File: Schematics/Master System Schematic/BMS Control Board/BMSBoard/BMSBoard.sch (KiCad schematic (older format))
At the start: 22 parts, among them J1 GLV_PWR, J10 GND_QC, J2 GLV_Signal, J3 Charge_PWR, J4 Charge_Signal, J5 PumpIO, J6 Therm_PWR, J7 Therm_Signal, J8 BMS_PWR, J9 BMS_Signal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

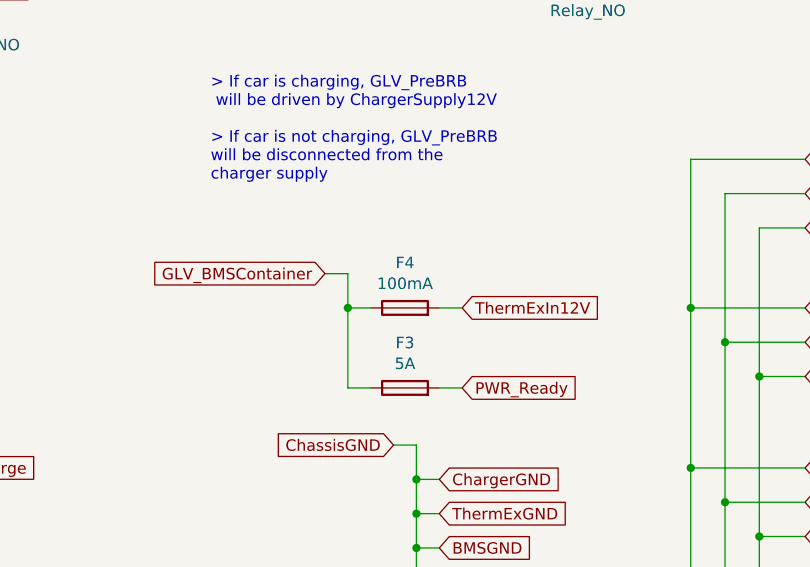
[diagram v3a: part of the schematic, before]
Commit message: Small fuse change
> Removed fuse for thermistor expansion
Version 2.2
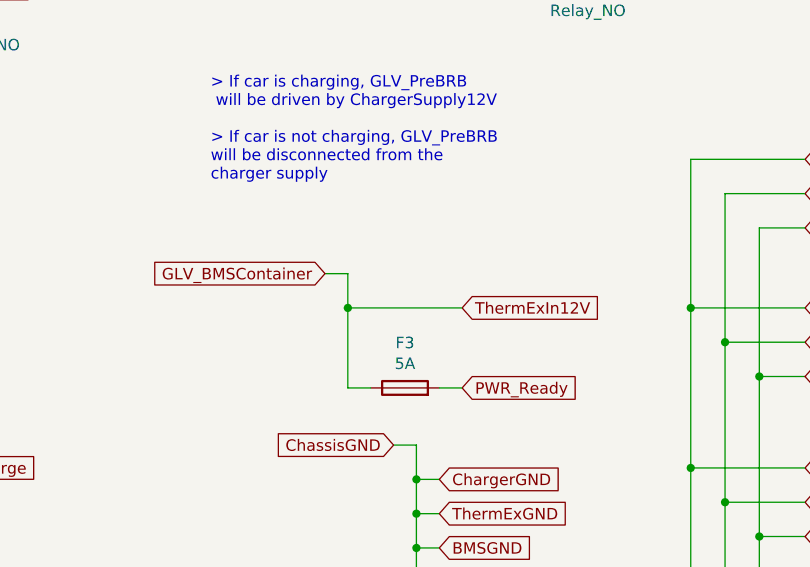
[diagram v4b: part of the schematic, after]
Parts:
- removed F4: 100mA, symbol Device:Fuse
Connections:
- net ThermExIn12V is gone; now on net GLV_BMSContainer: J6.1 (Pin_1)
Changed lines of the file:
@@
 Sheet 1 1
 Title "BMS Control Board"
-Date "2020-11-14"
-Rev "2.1"
+Date "2020-11-19"
+Rev "2.2"
 Comp "Northeastern Electric Racing"
 Comment1 "https://github.com/Northeastern-Electric-Racing/NER"
@@
 	6250 4050 6350 4050
 Wire Wire Line
-	6450 4200 6350 4200
-Wire Wire Line
 	6350 4200 6350 4050
 Text GLabel 6550 4800 0    50   Input ~ 0
@@
 Wire Wire Line
 	6750 4550 6850 4550
-$Comp
-L Device:Fuse F4
-U 1 1 5FB1D8F5
-P 6600 4200
-F 0 "F4" V 6797 4200 50  0000 C CNN
-F 1 "100mA" V 6706 4200 50  0000 C CNN
-F 2 "" V 6530 4200 50  0001 C CNN
-F 3 "~" H 6600 4200 50  0001 C CNN
-	1    6600 4200
-	0    -1   -1   0
-$EndComp
-Wire Wire Line
-	6750 4200 6850 4200
+Wire Wire Line
+	6350 4200 6850 4200
 $EndSCHEMATC

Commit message: Minor Fixes
> Fixed some minor issues
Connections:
- no-connect marks 1 -> 2
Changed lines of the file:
@@
 $EndComp
-Wire Wire Line
-	6650 5250 6650 5400
-Text GLabel 6750 5400 2    50   Input ~ 0
-FanGND
-Wire Wire Line
-	6750 5400 6650 5400
-Connection ~ 6650 5400
-Wire Wire Line
-	6650 5400 6650 5550
 Wire Wire Line
 	7300 5550 6650 5550
@@
 Wire Wire Line
 	6350 4200 6850 4200
+Wire Wire Line
+	6650 5250 6650 5550
+NoConn ~ 1000 1500
 $EndSCHEMATC

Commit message: Minor fuse change
> Moved F2 to the other side of the relay.
Version 2.3
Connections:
- net ChargerSupply12V: now also K2.2; no longer F2.1
- net PWR_Charge: now also F2.2; no longer K2.3
- new net: F2.1, K2.3
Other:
- moved on the sheet: F2
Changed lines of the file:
@@
 Sheet 1 1
 Title "BMS Control Board"
-Date "2020-11-19"
-Rev "2.2"
+Date "2020-11-23"
+Rev "2.3"
 Comp "Northeastern Electric Racing"
 Comment1 "https://github.com/Northeastern-Electric-Racing/NER"
@@
 Wire Notes Line
 	2500 1250 2500 6000
-Text GLabel 3550 4900 0    50   Input ~ 0
+Text GLabel 3850 4900 0    50   Input ~ 0
 ChargerSupply12V
-Text GLabel 4450 4900 2    50   Input ~ 0
+Text GLabel 4900 4900 2    50   Input ~ 0
 PWR_Charge
 $Comp
@@
 L Device:Fuse F2
 U 1 1 5FB0792D
-P 3700 4900
-F 0 "F2" V 3897 4900 50  0000 C CNN
-F 1 "5A" V 3806 4900 50  0000 C CNN
-F 2 "" V 3630 4900 50  0001 C CNN
-F 3 "~" H 3700 4900 50  0001 C CNN
-	1    3700 4900
+P 4750 4900
+F 0 "F2" V 4947 4900 50  0000 C CNN
+F 1 "5A" V 4856 4900 50  0000 C CNN
+F 2 "" V 4680 4900 50  0001 C CNN
+F 3 "~" H 4750 4900 50  0001 C CNN
+	1    4750 4900
 	0    -1   -1   0
 $EndComp
@@
 	6650 5250 6650 5550
 NoConn ~ 1000 1500
+Wire Wire Line
+	4450 4900 4600 4900
 $EndSCHEMATC

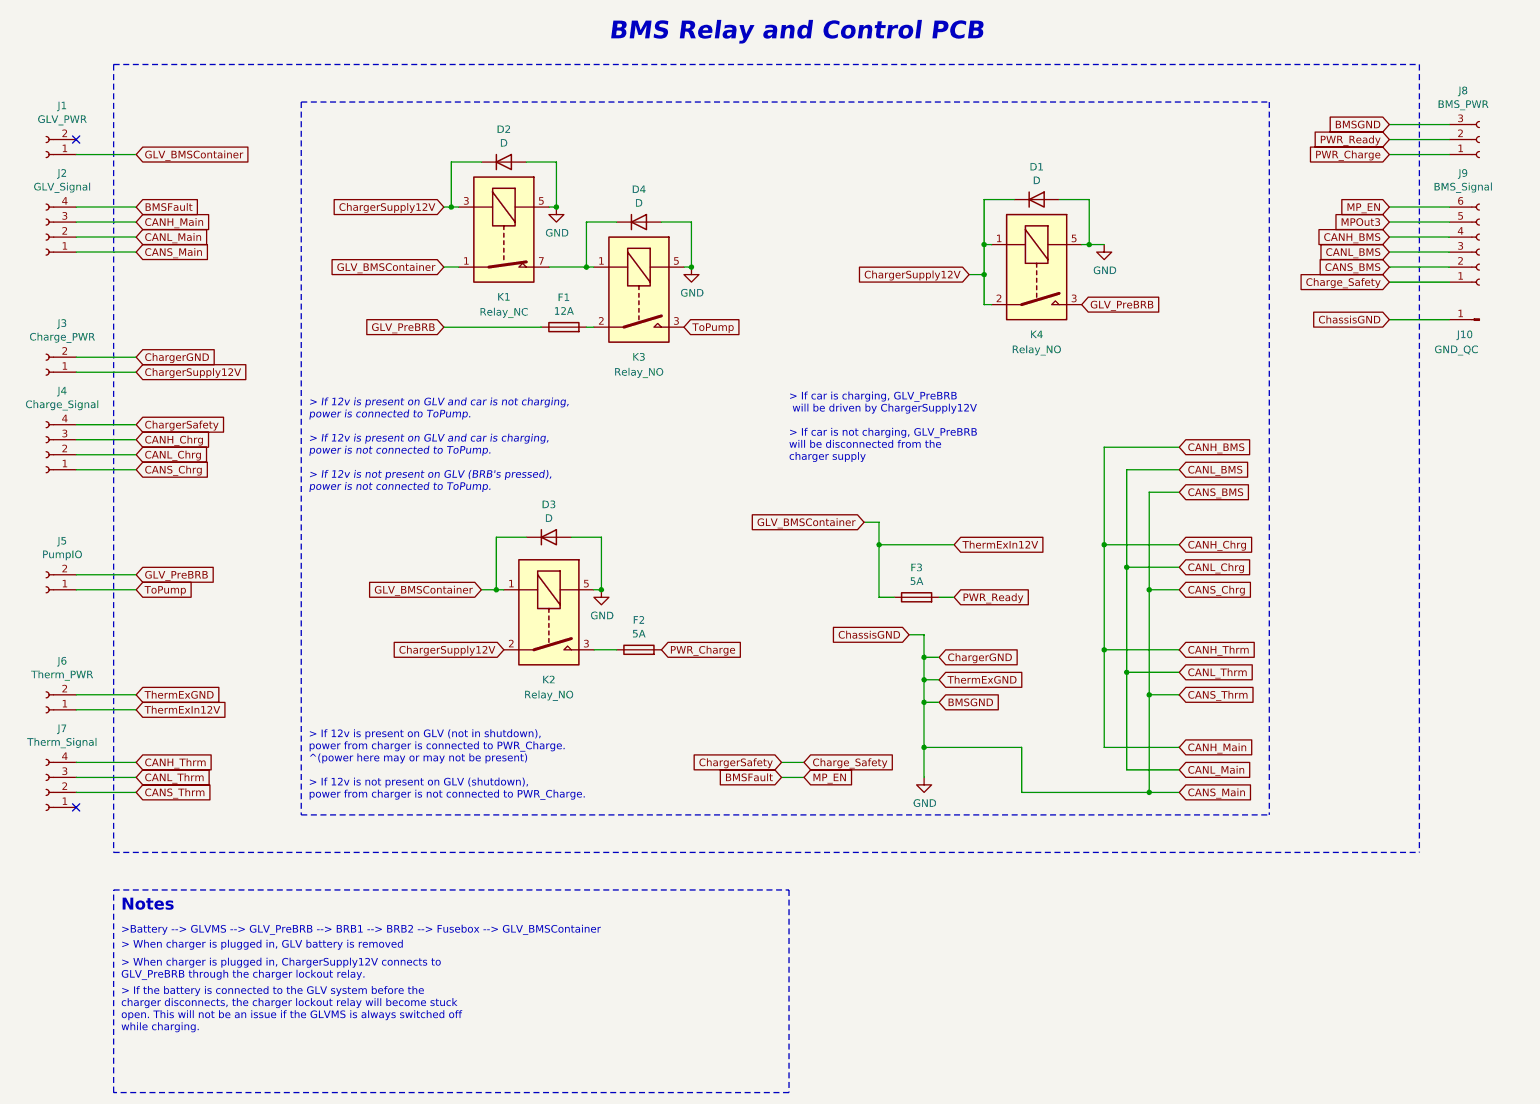
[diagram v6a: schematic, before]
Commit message: Stylistic changes and size consolidation
> Combined GLV_PWR and Charge_PWR into the 3 pin connector GLV/Charge_PWR
> Replaced K4 with a schottky diode (D1)
> Major sytlistic changes, replaced net labels with wires

Version 3.0
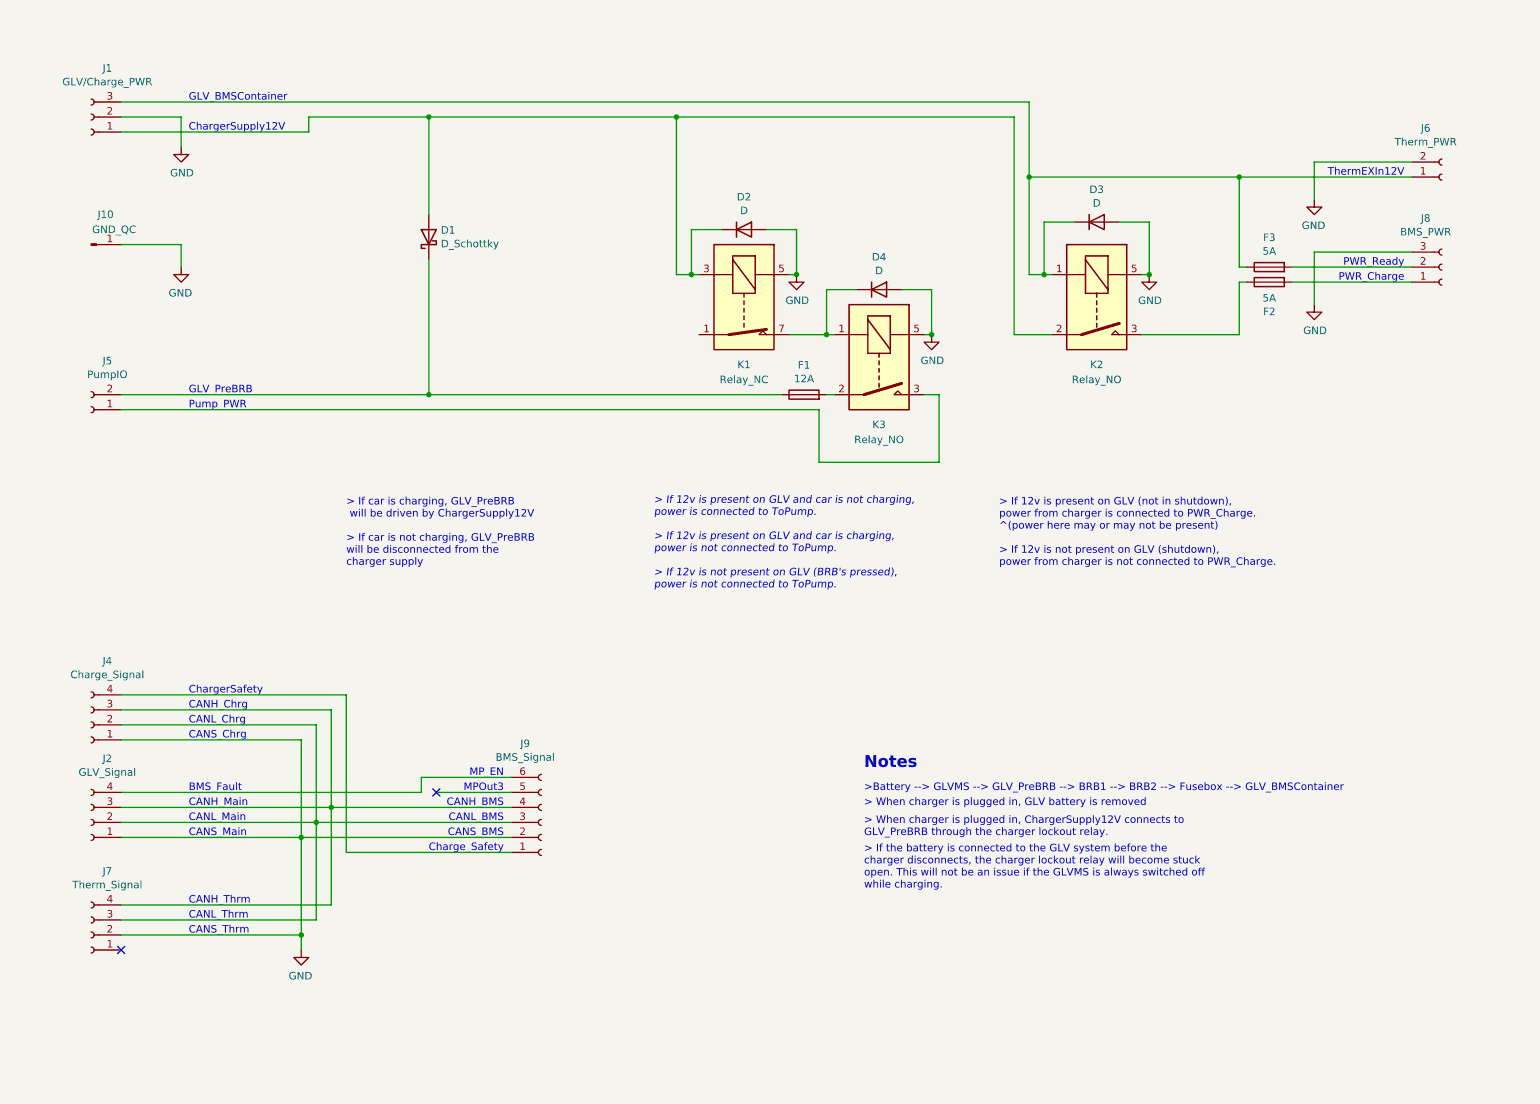
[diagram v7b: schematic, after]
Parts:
- removed D1: D, symbol Device:D
- removed J1: GLV_PWR, symbol Connector:Conn_01x02_Female
- removed J3: Charge_PWR, symbol Connector:Conn_01x02_Female
- removed K4: Relay_NO, Relay_THT:Relay_SPST_Omron-G5Q-1A, symbol Relay:G5Q-1A
- added D1: D_Schottky, symbol Device:D_Schottky
- added J1: GLV/Charge_PWR, symbol Connector:Conn_01x03_Female
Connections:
- net GND: now also J1.2 (Pin_2)
- net BMSFault: no longer names the net of J2.4 (Pin_4), J9.6 (Pin_6)
- net CANH_BMS: no longer names the net of J2.3 (Pin_3), J4.3 (Pin_3), J7.4 (Pin_4), J9.4 (Pin_4)
- net CANL_BMS: no longer names the net of J2.2 (Pin_2), J4.2 (Pin_2), J7.3 (Pin_3), J9.3 (Pin_3)
- net Charge_Safety: no longer names the net of J4.4 (Pin_4), J9.1 (Pin_1)
- net ChargerSupply12V: no longer names the net of D2.1 (K), K1.3, K2.2
- net ChargerSupply12V: now also D1.2 (A), J1.1 (Pin_1)
- net GLV_BMSContainer: no longer names the net of D3.1 (K), F3.1, J6.1 (Pin_1), K2.1
- net GLV_BMSContainer: now also J1.3 (Pin_3); no longer K1.1
- net GLV_PreBRB: no longer names the net of F1.1, J5.2 (Pin_2)
- net GLV_PreBRB: now also D1.1 (K)
- net MPOut3: no longer names the net of J9.5 (Pin_5)
- net PWR_Charge: no longer names the net of F2.2, J8.1 (Pin_1)
- net PWR_Ready: no longer names the net of F3.2, J8.2 (Pin_2)
- net ToPump: no longer names the net of J5.1 (Pin_1), K3.3
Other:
- note added: "BMS_Fault"
- note added: "CANH_BMS"
- note added: "CANH_Chrg"
- note added: "CANH_Main"
- note added: "CANH_Thrm"
- note added: "CANL_BMS"
- note added: "CANL_Chrg"
- note added: "CANL_Main"
- note added: "CANL_Thrm"
- note added: "CANS_BMS"
- note added: "CANS_Chrg"
- note added: "CANS_Main"
- note added: "CANS_Thrm"
- note added: "Charge_Safety"
- note added: "ChargerSafety\n"
- note added: "ChargerSupply12V"
- note added: "GLV_BMSContainer\n"
- note added: "GLV_PreBRB\n"
- note added: "MPOut3"
- note added: "MP_EN"
- note added: "PWR_Charge"
- note added: "PWR_Ready"
- note added: "Pump_PWR\n"
- note added: "ThermEXIn12V"
- note removed: "BMS Relay and Control PCB\n"
- moved on the sheet: D2, D3, D4, F1, F2, F3, J10, J2, J4, J5, J6, J7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

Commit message: Minor fixes and pin changes
> Fixed connection to K1
> Changed pin order on BMS_Signal, Therm_Signal, GLV/Charge_PWR, BMS_PWR

Version 3.1
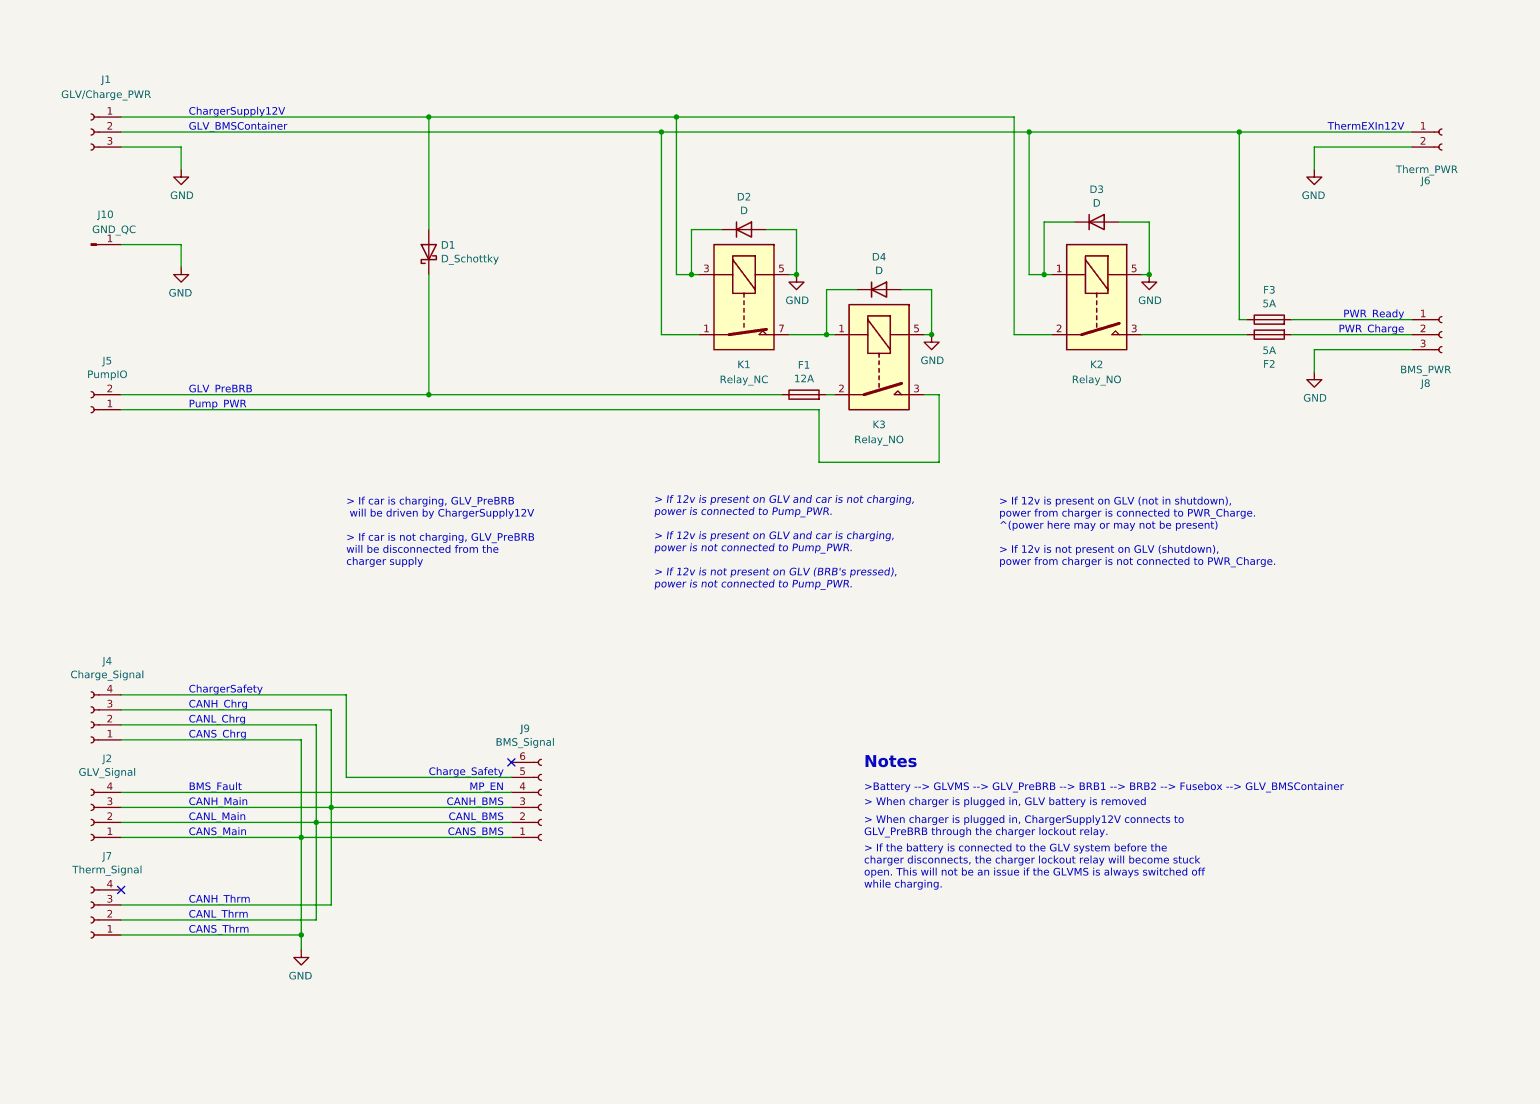
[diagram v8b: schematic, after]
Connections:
- net GND: now also J1.3 (Pin_3), J7.1 (Pin_1), J9.1 (Pin_1); no longer J1.2 (Pin_2), J7.2 (Pin_2), J9.2 (Pin_2)
- net at F2.2: now also J8.2 (Pin_2); no longer J8.1 (Pin_1)
- net at D3.1 (K), F3.1, J6.1 (Pin_1)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: now also J1.2 (Pin_2), K1.1; no longer J1.3 (Pin_3)
- net at F3.2: now also J8.1 (Pin_1); no longer J8.2 (Pin_2)
- net at J2.2 (Pin_2), J4.2 (Pin_2): now also J7.2 (Pin_2), J9.2 (Pin_2); no longer J7.3 (Pin_3), J9.3 (Pin_3)
- net at J2.3 (Pin_3), J4.3 (Pin_3): now also J7.3 (Pin_3), J9.3 (Pin_3); no longer J7.4 (Pin_4), J9.4 (Pin_4)
- net at J2.4 (Pin_4): now also J9.4 (Pin_4); no longer J9.6 (Pin_6)
- net at J4.4 (Pin_4): now also J9.5 (Pin_5); no longer J9.1 (Pin_1)
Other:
- note added: "> If 12v is present on GLV and car is not charging, \npower is connected to Pump_PWR.\n\n> If 12v is present on GLV and car is charging, \npower is not connected to Pump_PWR.\n\n> If 12v is not present on GLV (BRB's pressed),\npower is not connected to Pump_PWR."
- note removed: "> If 12v is present on GLV and car is not charging, \npower is connected to ToPump.\n\n> If 12v is present on GLV and car is charging, \npower is not connected to ToPump.\n\n> If 12v is not present on GLV (BRB's pressed),\npower is not connected to ToPump."
- note removed: "MPOut3"
- moved on the sheet: D1, F2, F3, J1, J6, J7, J8, J9
